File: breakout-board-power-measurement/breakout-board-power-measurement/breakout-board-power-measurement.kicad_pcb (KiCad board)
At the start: 2 copper layers, 62 parts, among them J1 Screw_Terminal_01x04, J2 Conn_01x09, J3 Conn_01x07, J4 Conn_01x02, U1 MCP3911A0-E-SS, U2 Si8641BA-B-IU, U3 LM317_TO-252, Y1 10M

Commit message: ...
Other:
- board outline added: 70.6 x 40.2 mm
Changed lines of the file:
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@@
     )
   )
+  (gr_rect (start 118.4 112.6) (end 189 152.8)
+    (stroke (width 0.1) (type default)) (fill none) (layer "Edge.Cuts"))
   (gr_text "C8" (at 173.228 150.0257 180) (layer "F.Fab")
     (effects (font (size 0.8 0.8) (thickness 0.12)))
@@
         (xy 144.653 124.079)
         (xy 144.653 116.0018)
-        (xy 111.506 116.0018)
-        (xy 111.506 152.654)
+        (xy 118.706 116.0018)
+        (xy 118.706 152.654)
         (xy 148.209 152.654)
       )

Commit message: ...
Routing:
- net GNDD: track 161.8 -> 163.7 mm
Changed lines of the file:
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@@
   (segment (start 150.241 117.856) (end 153.797 114.3) (width 0.8) (layer "F.Cu") (net 8))
   (segment (start 170.2564 142.0876) (end 170.231 142.113) (width 0.6) (layer "F.Cu") (net 8))
-  (via (at 174.3964 148.6154) (size 1.2) (drill 0.8) (layers "F.Cu" "B.Cu") (free) (net 8))
+  (via (at 176.4 148.8) (size 1.2) (drill 0.8) (layers "F.Cu" "B.Cu") (free) (net 8))
   (via (at 150.241 117.856) (size 1.2) (drill 0.8) (layers "F.Cu" "B.Cu") (free) (net 8))
   (via (at 175.514 126.111) (size 1.2) (drill 0.8) (layers "F.Cu" "B.Cu") (free) (net 8))
@@
   (via (at 172.1104 142.0876) (size 1.2) (drill 0.8) (layers "F.Cu" "B.Cu") (free) (net 8))
   (segment (start 147.747057 114.681) (end 140.335 114.681) (width 0.8) (layer "B.Cu") (net 8))
+  (segment (start 174.8828 150.3172) (end 176.4 148.8) (width 1) (layer "B.Cu") (net 8))
   (segment (start 151.3959 150.0628) (end 149.7584 148.4253) (width 1) (layer "B.Cu") (net 8))
-  (segment (start 173.0248 142.0876) (end 172.1104 142.0876) (width 0.6) (layer "B.Cu") (net 8))
   (segment (start 132.8934 141.0202) (end 131.5212 142.3924) (width 1) (layer "B.Cu") (net 8))
   (segment (start 175.514 123.633) (end 175.514 126.111) (width 0.6) (layer "B.Cu") (net 8))
   (segment (start 133.7572 136.652) (end 133.7572 132.1506) (width 1) (layer "B.Cu") (net 8))
-  (segment (start 174.3964 143.4592) (end 173.0248 142.0876) (width 0.6) (layer "B.Cu") (net 8))
-  (segment (start 174.3964 148.6154) (end 174.3964 143.4592) (width 0.6) (layer "B.Cu") (net 8))
   (segment (start 131.5212 148.4884) (end 131.4704 148.5392) (width 1) (layer "B.Cu") (net 8))
   (segment (start 150.241 117.174943) (end 147.747057 114.681) (width 0.8) (layer "B.Cu") (net 8))
@@
   (segment (start 184.277 151.003) (end 185.674 151.003) (width 1) (layer "B.Cu") (net 8))
   (segment (start 174.3964 150.3172) (end 174.3964 150.3934) (width 1) (layer "B.Cu") (net 8))
-  (segment (start 174.3964 150.3172) (end 174.3964 148.6154) (width 1) (layer "B.Cu") (net 8))
   (segment (start 133.9088 136.8036) (end 133.7572 136.652) (width 1) (layer "B.Cu") (net 8))
   (segment (start 183.642 151.638) (end 184.277 151.003) (width 1) (layer "B.Cu") (net 8))
   (segment (start 134.6462 139.6754) (end 133.9088 138.938) (width 1) (layer "B.Cu") (net 8))
+  (segment (start 173.0248 142.0876) (end 172.1104 142.0876) (width 0.6) (layer "B.Cu") (net 8))
   (segment (start 150.241 117.856) (end 150.241 117.174943) (width 0.8) (layer "B.Cu") (net 8))
   (segment (start 134.6462 141.0202) (end 134.6462 139.6754) (width 1) (layer "B.Cu") (net 8))
+  (segment (start 174.3964 143.4592) (end 173.0248 142.0876) (width 0.6) (layer "B.Cu") (net 8))
   (segment (start 134.6462 141.0202) (end 132.8934 141.0202) (width 1) (layer "B.Cu") (net 8))
   (segment (start 131.4704 148.5392) (end 132.6896 149.7584) (width 1) (layer "B.Cu") (net 8))
   (segment (start 133.7572 132.1506) (end 134.0818 131.826) (width 1) (layer "B.Cu") (net 8))
   (segment (start 155.4484 151.892) (end 172.8216 151.892) (width 1) (layer "B.Cu") (net 8))
+  (segment (start 174.3964 146.7964) (end 174.3964 143.4592) (width 0.6) (layer "B.Cu") (net 8))
   (segment (start 184.8612 123.6472) (end 183.1482 123.6472) (width 0.6) (layer "B.Cu") (net 8))
   (segment (start 140.335 114.681) (end 134.0818 120.9342) (width 0.8) (layer "B.Cu") (net 8))
   (segment (start 174.3964 150.3934) (end 175.641 151.638) (width 1) (layer "B.Cu") (net 8))
   (segment (start 183.1482 123.6472) (end 183.134 123.633) (width 0.6) (layer "B.Cu") (net 8))
+  (segment (start 176.4 148.8) (end 174.3964 146.7964) (width 0.6) (layer "B.Cu") (net 8))
   (segment (start 153.6192 150.0628) (end 155.4484 151.892) (width 1) (layer "B.Cu") (net 8))
   (segment (start 175.641 151.638) (end 183.642 151.638) (width 1) (layer "B.Cu") (net 8))
@@
   (segment (start 148.336 149.7584) (end 149.7076 148.3868) (width 1) (layer "B.Cu") (net 8))
   (segment (start 132.6896 149.7584) (end 148.336 149.7584) (width 1) (layer "B.Cu") (net 8))
+  (segment (start 174.3964 150.3172) (end 174.8828 150.3172) (width 1) (layer "B.Cu") (net 8))
   (segment (start 168.402 137.668) (end 169.869998 136.200002) (width 0.4) (layer "F.Cu") (net 9))
   (segment (start 165.5096 148.9589) (end 165.0139 148.4632) (width 0.4) (layer "F.Cu") (net 9))
@@
   (segment (start 134.696295 133.1575) (end 132.0145 133.1575) (width 0.8) (layer "F.Cu") (net 36))
   (segment (start 140.475 146.177) (end 137.795 146.177) (width 0.8) (layer "F.Cu") (net 36))
-  (segment (start 141.638 140.8) (end 140.081 139.243) (width 0.8) (layer "F.Cu") (net 37))
+  (segment (start 141.638 140.8) (end 139.192 138.354) (width 0.8) (layer "F.Cu") (net 37))
+  (segment (start 137.795 126.873) (end 136.957 126.873) (width 0.8) (layer "F.Cu") (net 37))
+  (segment (start 138.303 127.381) (end 137.795 126.873) (width 0.8) (layer "F.Cu") (net 37))
+  (segment (start 141.638 140.8) (end 141.557 140.8) (width 0.8) (layer "F.Cu") (net 37))
+  (segment (start 138.303 132.715) (end 138.303 127.381) (width 0.8) (layer "F.Cu") (net 37))
   (segment (start 139.192 133.604) (end 138.303 132.715) (width 0.8) (layer "F.Cu") (net 37))
-  (segment (start 138.303 127.381) (end 137.795 126.873) (width 0.8) (layer "F.Cu") (net 37))
-  (segment (start 139.192 136.017) (end 140.081 136.906) (width 0.8) (layer "F.Cu") (net 37))
-  (segment (start 137.795 126.873) (end 136.957 126.873) (width 0.8) (layer "F.Cu") (net 37))
-  (segment (start 140.081 139.243) (end 140.081 136.906) (width 0.8) (layer "F.Cu") (net 37))
-  (segment (start 138.303 132.715) (end 138.303 127.381) (width 0.8) (layer "F.Cu") (net 37))
-  (segment (start 139.192 136.017) (end 139.192 133.604) (width 0.8) (layer "F.Cu") (net 37))
-  (segment (start 141.638 140.8) (end 141.557 140.8) (width 0.8) (layer "F.Cu") (net 37))
+  (segment (start 139.192 138.354) (end 139.192 133.604) (width 0.8) (layer "F.Cu") (net 37))
   (segment (start 140.475 148.717) (end 134.9395 148.717) (width 0.8) (layer "F.Cu") (net 38))
   (segment (start 125.476 146.533) (end 125.476 143.764) (width 2.5) (layer "F.Cu") (net 38))

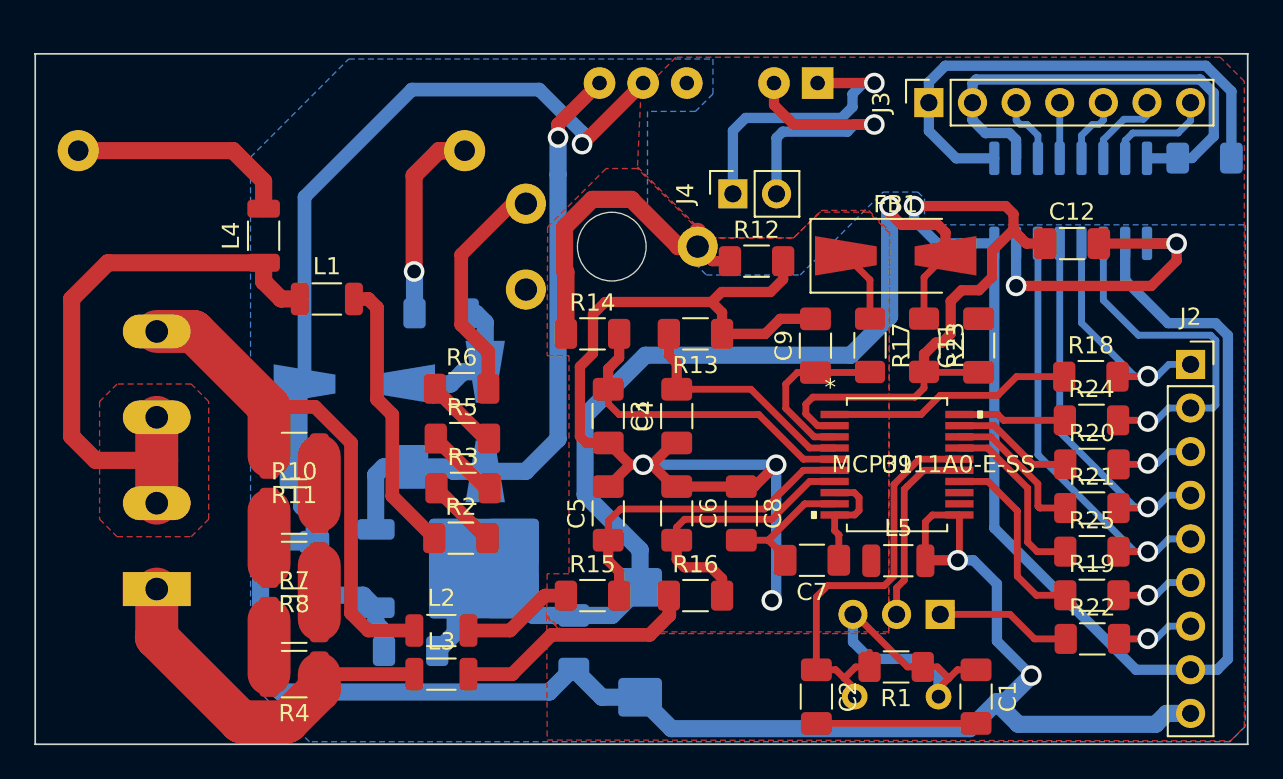
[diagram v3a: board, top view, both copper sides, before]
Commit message: Changed vias to test points
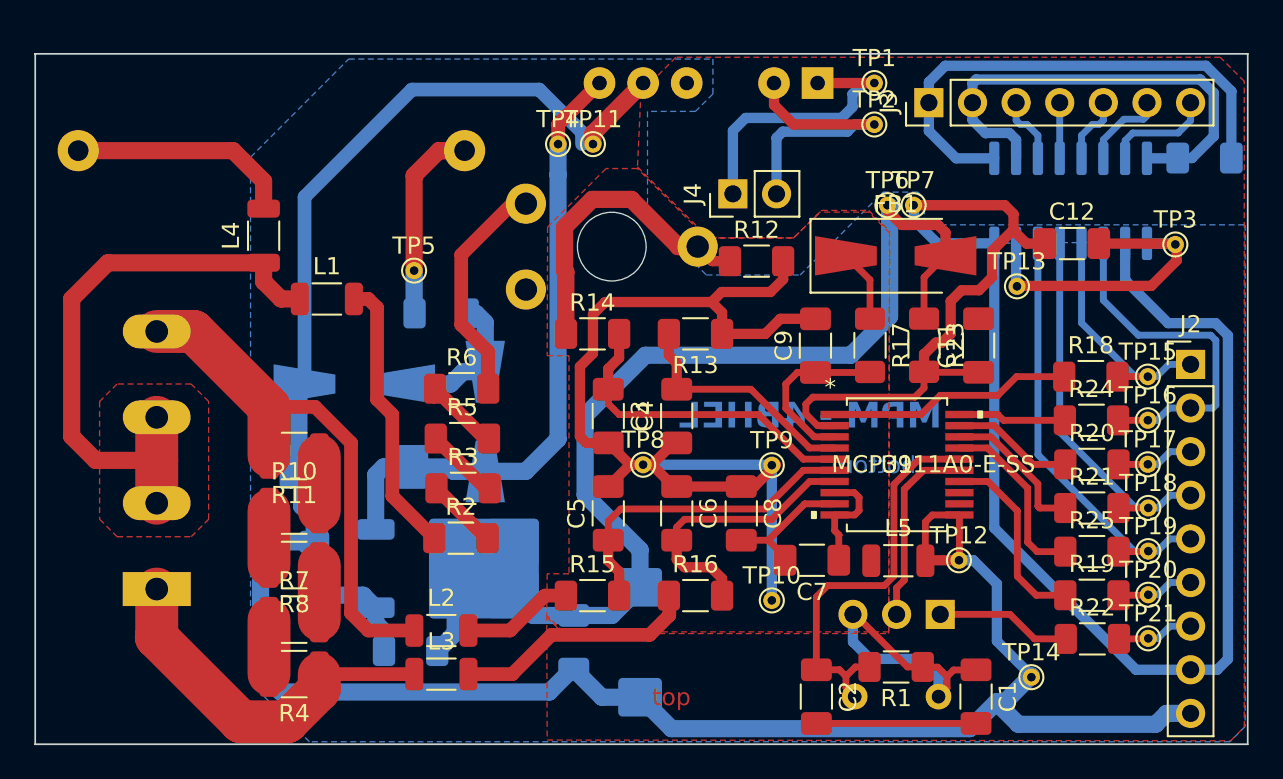
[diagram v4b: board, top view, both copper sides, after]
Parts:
- added TP1: TestPoint, TestPoint:TestPoint_THTPad_D1.0mm_Drill0.5mm, F.Cu at (167.3, 114.3)
- added TP10: TestPoint, TestPoint:TestPoint_THTPad_D1.0mm_Drill0.5mm, F.Cu at (161.3, 144.4)
- added TP11: TestPoint, TestPoint:TestPoint_THTPad_D1.0mm_Drill0.5mm, F.Cu at (150.9, 117.9)
- added TP12: TestPoint, TestPoint:TestPoint_THTPad_D1.0mm_Drill0.5mm, F.Cu at (172.2, 142.1)
- added TP13: TestPoint, TestPoint:TestPoint_THTPad_D1.0mm_Drill0.5mm, F.Cu at (175.6, 126.1)
- added TP14: TestPoint, TestPoint:TestPoint_THTPad_D1.0mm_Drill0.5mm, F.Cu at (176.4, 148.9)
- added TP15: TestPoint, TestPoint:TestPoint_THTPad_D1.0mm_Drill0.5mm, F.Cu at (183.2, 131.4)
- added TP16: TestPoint, TestPoint:TestPoint_THTPad_D1.0mm_Drill0.5mm, F.Cu at (183.2, 133.9)
- added TP17: TestPoint, TestPoint:TestPoint_THTPad_D1.0mm_Drill0.5mm, F.Cu at (183.2, 136.5)
- added TP18: TestPoint, TestPoint:TestPoint_THTPad_D1.0mm_Drill0.5mm, F.Cu at (183.2, 139.0)
- added TP19: TestPoint, TestPoint:TestPoint_THTPad_D1.0mm_Drill0.5mm, F.Cu at (183.2, 141.6)
- added TP2: TestPoint, TestPoint:TestPoint_THTPad_D1.0mm_Drill0.5mm, F.Cu at (167.3, 116.7)
- added TP20: TestPoint, TestPoint:TestPoint_THTPad_D1.0mm_Drill0.5mm, F.Cu at (183.2, 144.1)
- added TP21: TestPoint, TestPoint:TestPoint_THTPad_D1.0mm_Drill0.5mm, F.Cu at (183.2, 146.6)
- added TP3: TestPoint, TestPoint:TestPoint_THTPad_D1.0mm_Drill0.5mm, F.Cu at (184.8, 123.7)
- added TP4: TestPoint, TestPoint:TestPoint_THTPad_D1.0mm_Drill0.5mm, F.Cu at (148.8, 117.9)
- added TP5: TestPoint, TestPoint:TestPoint_THTPad_D1.0mm_Drill0.5mm, F.Cu at (140.5, 125.2)
- added TP6: TestPoint, TestPoint:TestPoint_THTPad_D1.0mm_Drill0.5mm, F.Cu at (168.0, 121.4)
- added TP7: TestPoint, TestPoint:TestPoint_THTPad_D1.0mm_Drill0.5mm, F.Cu at (169.5, 121.4)
- added TP8: TestPoint, TestPoint:TestPoint_THTPad_D1.0mm_Drill0.5mm, F.Cu at (153.8, 136.5)
- added TP9: TestPoint, TestPoint:TestPoint_THTPad_D1.0mm_Drill0.5mm, F.Cu at (161.3, 136.6)
- J2: footprint Connector_PinSocket_2.54mm:PinSocket_1x09_P2.54mm_Vertical -> Connector_PinHeader_2.54mm:PinHeader_1x09_P2.54mm_Vertical
- J3: footprint Connector_PinSocket_2.54mm:PinSocket_1x07_P2.54mm_Vertical -> Connector_PinHeader_2.54mm:PinHeader_1x07_P2.54mm_Vertical
- J4: footprint Connector_PinSocket_2.54mm:PinSocket_1x02_P2.54mm_Vertical -> Connector_PinHeader_2.54mm:PinHeader_1x02_P2.54mm_Vertical
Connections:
- net Net-(C10-Pad2) renamed /x_cap_out
- net Net-(D2-K) renamed /LM317_Vin
- net Net-(J2-Pin_1) renamed /~{RESET}_
- net Net-(J2-Pin_2) renamed /SDO_
- net Net-(J2-Pin_3) renamed /SDI_
- net Net-(J2-Pin_4) renamed /SCK_
- net Net-(J2-Pin_5) renamed /~{CS}_
- net Net-(J2-Pin_6) renamed /~{DR}_
- net Net-(J2-Pin_7) renamed /OSC1_ext_
- net Net-(J4-Pin_1) renamed /5V_ext
- net Net-(J4-Pin_2) renamed /GND_ext
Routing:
- net /voltage_pos: track 20.5 -> 18.1 mm
- net /OSC2: track 24.8 -> 23.9 mm
- net /OSC1: track 19.2 -> 18.7 mm
- net /LM317_Vin: track 36.6 -> 36.2 mm, vias 1 -> 0
- net GNDA: track 68.0 -> 67.6 mm, vias 3 -> 0
- net GNDD: track 163.7 -> 163.5 mm, vias 5 -> 0
- net /SDO_: track 20.7 -> 20.6 mm, vias 1 -> 0
- net +3.3V: track 59.8 -> 59.9 mm, vias 1 -> 0
- net /SCK_: track 22.4 -> 22.3 mm, vias 1 -> 0
- net /SDI_: track 4.50 -> 4.45 mm, vias 1 -> 0
- net /3V3D: vias 1 -> 0
- net /OSC1_ext_: track 4.48 -> 4.44 mm, vias 1 -> 0
- net /~{CS}_: vias 1 -> 0
- net /~{DR}_: track 4.50 -> 4.47 mm, vias 1 -> 0
- net /~{RESET}_: vias 1 -> 0
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- added copper zone on B.Cu, net (none)
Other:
- board text added: "MPM - 4BHEL"
- board text added: "bottom"
- board text added: "top"

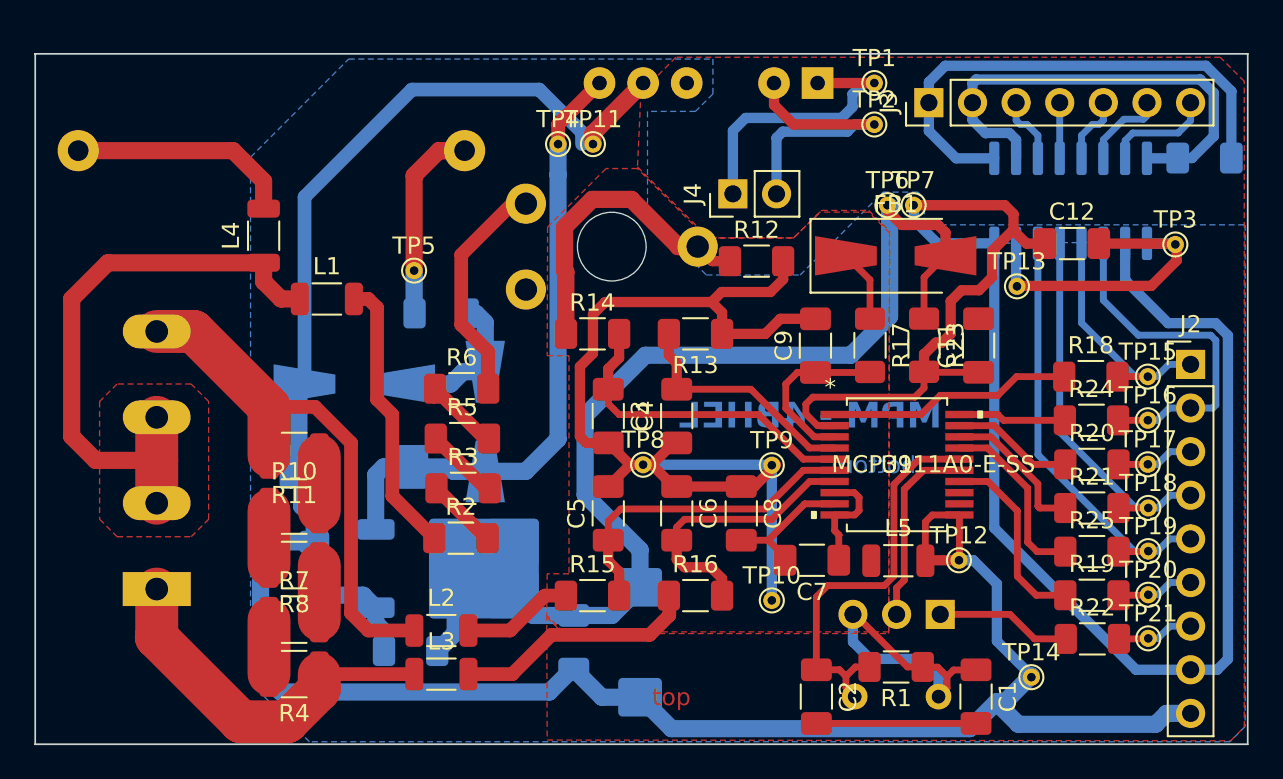
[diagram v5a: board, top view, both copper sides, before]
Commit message: Fixed Power Measurement PCB, important changes.
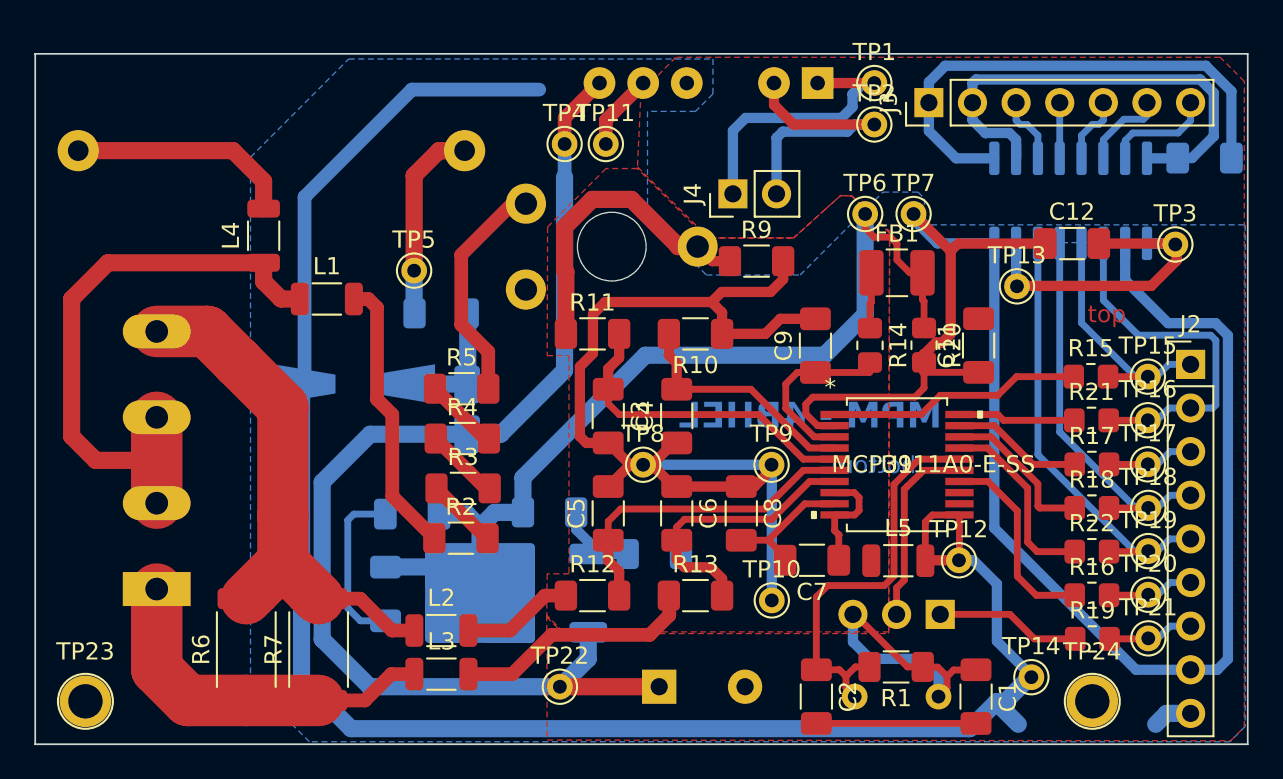
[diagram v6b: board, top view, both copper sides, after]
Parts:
- removed the R10 at (133.5, 139.2)
- removed the R11 at (133.5, 136.0)
- removed the R4 at (133.5, 148.7)
- removed the R8 at (133.5, 142.4)
- added R6: 50m, Resistor_SMD:R_2512_6332Metric, F.Cu at (130.7, 147.3)
- added TP22: TestPoint, Via:Via_THTPad_D1.5mm_Drill0.8mm, F.Cu at (148.9, 149.4)
- added TP23: TestPoint, Screwhole:Screwhole_THTPad_D3.0mm_Drill2.0mm, F.Cu at (121.3, 150.3)
- added TP24: TestPoint, Screwhole:Screwhole_THTPad_D3.0mm_Drill2.0mm, F.Cu at (179.9, 150.3)
- C1, C2: value 22p -> 18p
- C10: value 470n/530 -> 820n/530
- C13: footprint Capacitor_Tantalum_SMD:CP_EIA-7343-31_Kemet-D_Pad2.25x2.55mm_HandSolder -> Capacitor_THT:CP_Radial_D10.0mm_P5.00mm
- C15: value 10u/50 -> 10u; footprint Capacitor_Tantalum_SMD:CP_EIA-7343-31_Kemet-D_Pad2.25x2.55mm_HandSolder -> Capacitor_SMD:C_1206_3216Metric_Pad1.33x1.80mm_HandSolder
- D2: footprint Diode_SMD:D_SMA-SMB_Universal_Handsoldering -> Diode_SMD:D_MicroMELF_Handsoldering
- FB1: footprint Diode_SMD:D_SMA-SMB_Universal_Handsoldering -> Inductor_SMD:L_1210_3225Metric_Pad1.42x2.65mm_HandSolder
- R1: value 1M -> 1.2M
- R14: renamed from R17; footprint Resistor_SMD:R_1206_3216Metric_Pad1.30x1.75mm_HandSolder -> Resistor_SMD:R_0805_2012Metric_Pad1.20x1.40mm_HandSolder
- R15: renamed from R18; footprint Resistor_SMD:R_1206_3216Metric_Pad1.30x1.75mm_HandSolder -> Resistor_SMD:R_0805_2012Metric_Pad1.20x1.40mm_HandSolder
- R16: renamed from R19; footprint Resistor_SMD:R_1206_3216Metric_Pad1.30x1.75mm_HandSolder -> Resistor_SMD:R_0805_2012Metric_Pad1.20x1.40mm_HandSolder
- R17: renamed from R20; footprint Resistor_SMD:R_1206_3216Metric_Pad1.30x1.75mm_HandSolder -> Resistor_SMD:R_0805_2012Metric_Pad1.20x1.40mm_HandSolder
- R18: renamed from R21; footprint Resistor_SMD:R_1206_3216Metric_Pad1.30x1.75mm_HandSolder -> Resistor_SMD:R_0805_2012Metric_Pad1.20x1.40mm_HandSolder
- R19: renamed from R22; footprint Resistor_SMD:R_1206_3216Metric_Pad1.30x1.75mm_HandSolder -> Resistor_SMD:R_0805_2012Metric_Pad1.20x1.40mm_HandSolder
- R20: renamed from R23; footprint Resistor_SMD:R_1206_3216Metric_Pad1.30x1.75mm_HandSolder -> Resistor_SMD:R_0805_2012Metric_Pad1.20x1.40mm_HandSolder
- R21: renamed from R24; footprint Resistor_SMD:R_1206_3216Metric_Pad1.30x1.75mm_HandSolder -> Resistor_SMD:R_0805_2012Metric_Pad1.20x1.40mm_HandSolder
- R22: renamed from R25; footprint Resistor_SMD:R_1206_3216Metric_Pad1.30x1.75mm_HandSolder -> Resistor_SMD:R_0805_2012Metric_Pad1.20x1.40mm_HandSolder
- R24: renamed from R27; value 1k6 -> 1k5
- R25: renamed from R28; value 1k -> 910
- R7: footprint Resistor_SMD:R_1210_3225Metric -> Resistor_SMD:R_2512_6332Metric
- TP1, TP10, TP11, TP12, TP13, TP14, TP15, TP16, TP17, TP18, TP19, TP2, TP20, TP21, TP3, TP4, TP5, TP6, TP7, TP8, TP9: footprint TestPoint:TestPoint_THTPad_D1.0mm_Drill0.5mm -> Via:Via_THTPad_D1.5mm_Drill0.8mm
- moved C13 21.9 mm to (154.7, 149.4), turned to 0 degrees
- moved R24 19.8 mm to (154.4, 141.7), turned to 0 degrees
- moved C15 15.2 mm to (140.3, 139.4), turned to 180 degrees
- moved R25 11.4 mm to (148.3, 139.3), turned to 0 degrees
- moved C14 11.3 mm to (138.8, 144.1)
- moved U3 2.70 mm to (145.6, 144.0), turned to 180 degrees
- moved R7 2.25 mm to (134.9, 147.3), turned to 90 degrees
- moved TP6 1.39 mm to (166.7, 121.9)
- moved D2 1.27 mm to (143.6, 133.3)
- moved FB1 0.99 mm to (168.6, 125.3)
- moved TP11 0.75 mm to (151.6, 117.8)
- moved TP7 0.51 mm to (169.5, 121.9)
- moved TP4 0.38 mm to (149.2, 117.8)
- renumbered R13 to R10, R14 to R11, R15 to R12, R16 to R13, R26 to R23, R5 to R4, R6 to R5, R9 to R8, R12 to R9
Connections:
- R7 pad 1: Net-(R4-Pad2) (its old number) -> /current_neg
- R7 pad 2: Net-(R7-Pad2) -> /current_pos
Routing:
- net /LM317_Vin: track 36.2 -> 68.2 mm
- net GNDD: track 163.5 -> 155.4 mm
- net +3.3V: track 59.9 -> 54.9 mm
- net /3V3D: track 102.5 -> 98.8 mm
- net Net-(R7-Pad2): track 3.18 -> 0.00 mm
- net Net-(R4-Pad2) (its old number): track 3.18 -> 0.00 mm
- net Net-(R10-Pad2): track 3.18 -> 0.00 mm
- net Net-(R10-Pad1): track 3.17 -> 0.00 mm
- net Net-(U3-ADJ): track 6.60 -> 5.02 mm
- net Net-(D1-K): track 9.12 -> 7.83 mm
- removed copper zone on F.Cu, net HIGH_in
